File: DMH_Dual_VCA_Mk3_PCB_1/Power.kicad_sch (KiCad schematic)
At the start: 14 parts, among them J0 Conn_01x01, J100 IDC_02x05, U1 TL074, U2 TL074

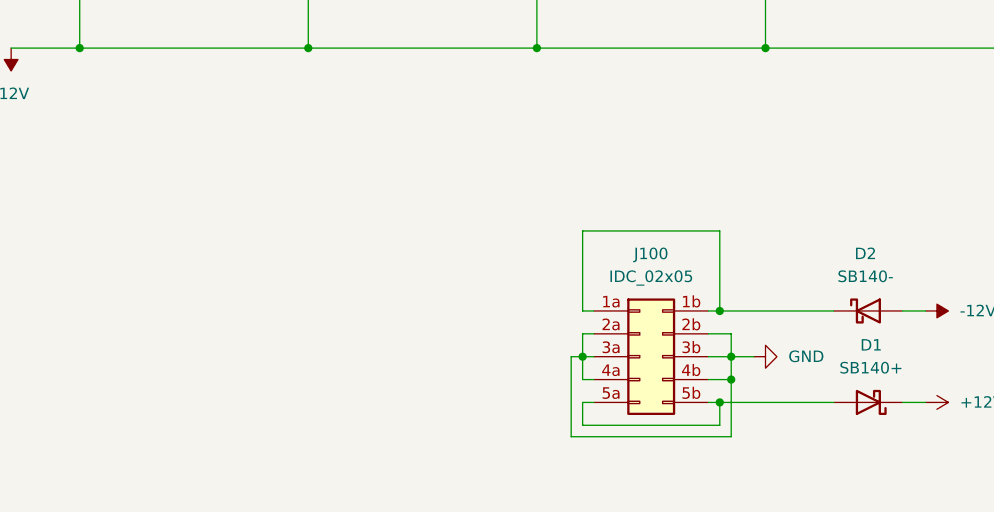
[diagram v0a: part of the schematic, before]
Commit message: Mode switching design in progress
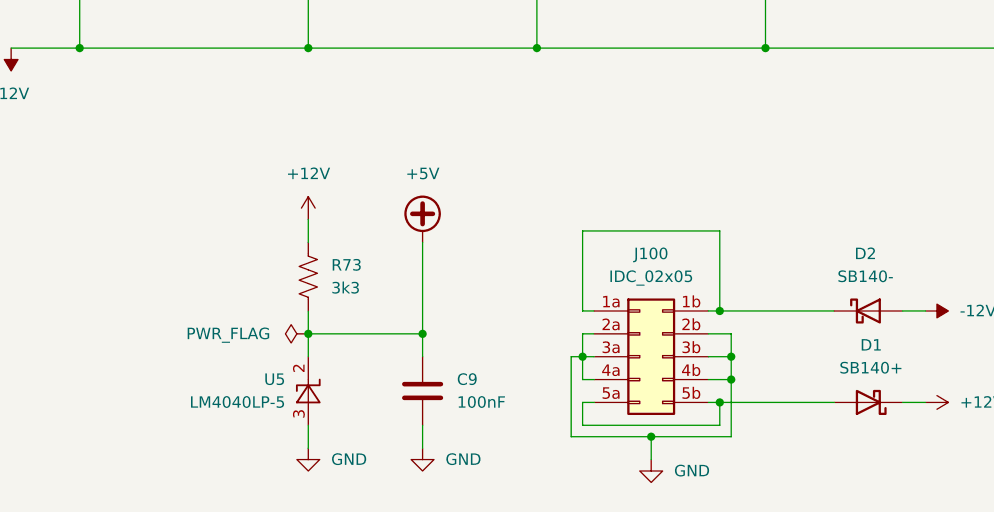
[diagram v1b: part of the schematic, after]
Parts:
- added C9: 100nF, Capacitor_THT:C_Disc_D4.3mm_W1.9mm_P5.00mm, symbol Device:C
- added R73: 3k3, Resistor_THT:R_Axial_DIN0207_L6.3mm_D2.5mm_P7.62mm_Horizontal, symbol Device:R_US
- added U5: LM4040LP-5, Package_TO_SOT_THT:TO-92_Inline, symbol Reference_Voltage:LM4040LP-5
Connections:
- net +12V: now also R73.2
- net GND: now also C9.2, U5.3 (A)
- new net +5V: C9.1, R73.1, U5.2 (K)

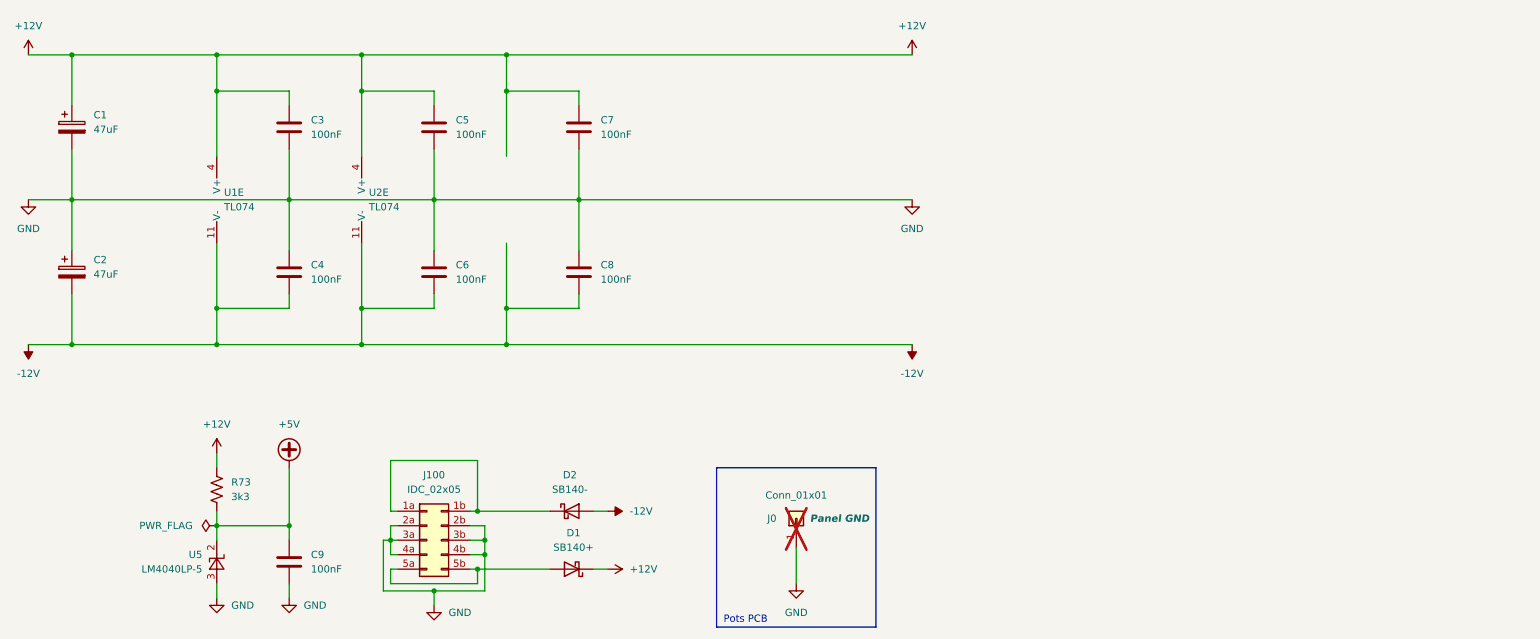
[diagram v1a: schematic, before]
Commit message: 2nd VCA design done
Clipping design in progress
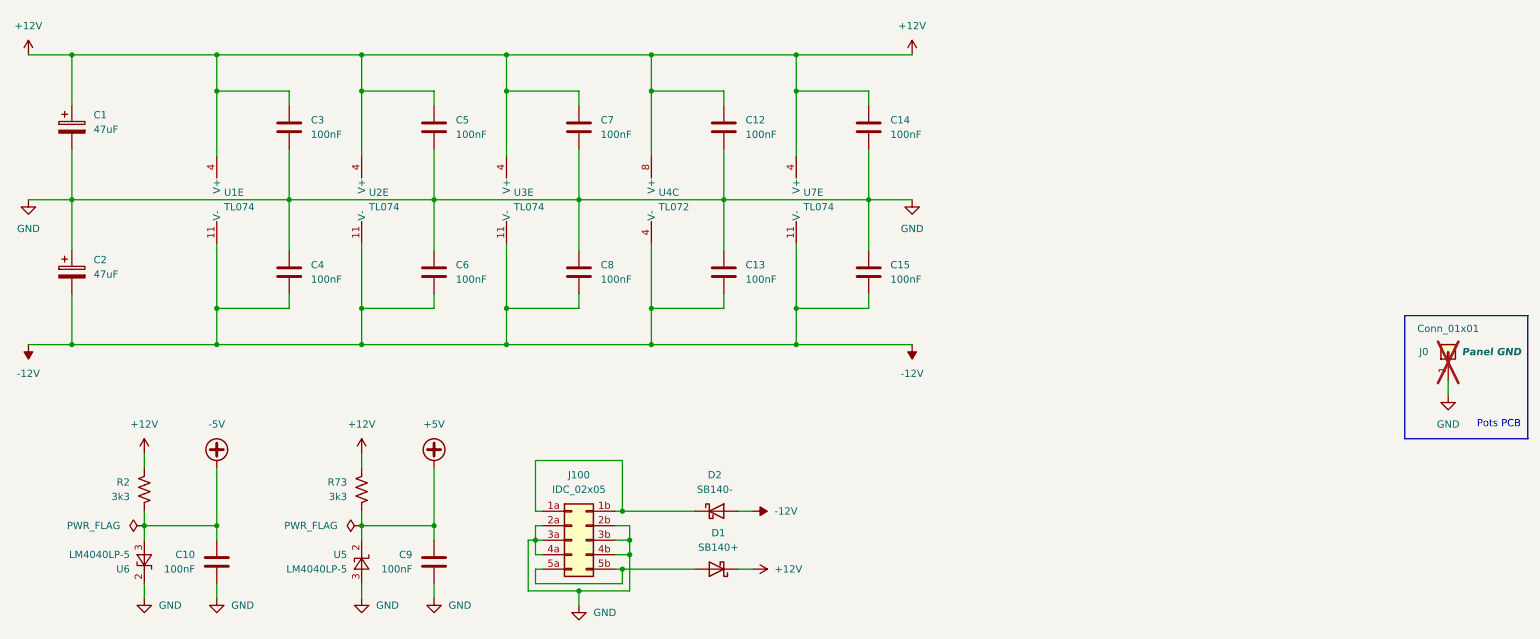
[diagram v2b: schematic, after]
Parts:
- added C10, C12, C13, C14, C15: 100nF, Capacitor_THT:C_Disc_D4.3mm_W1.9mm_P5.00mm, symbol Device:C
- added R2: 3k3, Resistor_THT:R_Axial_DIN0207_L6.3mm_D2.5mm_P7.62mm_Horizontal, symbol Device:R_US
- added U3, U7: TL074, Package_DIP:DIP-14_W7.62mm_Socket, symbol Amplifier_Operational:TL074
- added U4: TL072, Package_DIP:DIP-8_W7.62mm_Socket, symbol Amplifier_Operational:TL072
- added U6: LM4040LP-5, Package_TO_SOT_THT:TO-92_Inline, symbol Reference_Voltage:LM4040LP-5
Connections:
- net +12V: now also C12.1, C14.1, R2.2, U3.4 (V+), U4.8 (V+), U7.4 (V+)
- net -12V: now also C13.2, C15.2, U3.11 (V-), U4.4 (V-), U7.11 (V-)
- net GND: now also C10.2, C12.2, C13.1, C14.2, C15.1, U6.2 (K)
- new net -5V: C10.1, R2.1, U6.3 (A)
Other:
- moved on the sheet: C9, D1, D2, J0, J100, R73, U5

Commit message: Designed clip and dist circuit
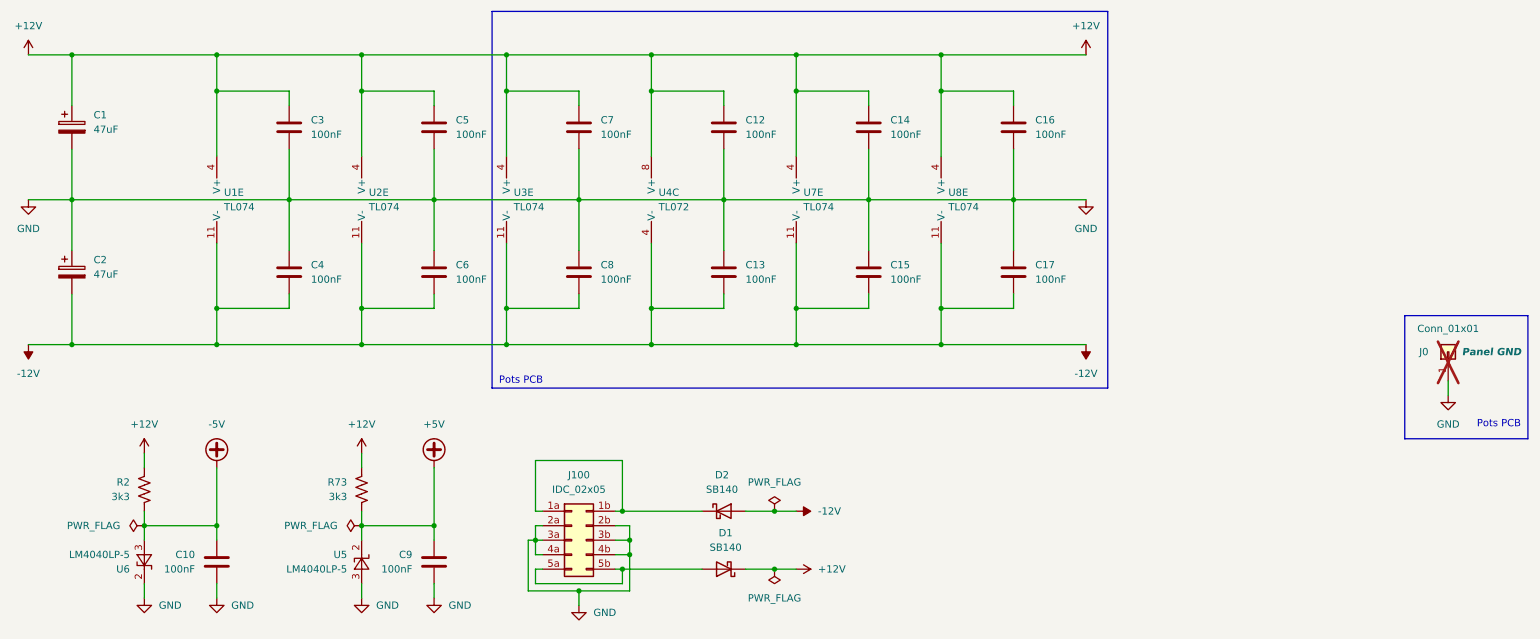
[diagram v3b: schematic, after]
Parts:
- added C16, C17: 100nF, Capacitor_THT:C_Disc_D4.3mm_W1.9mm_P5.00mm, symbol Device:C
- added U8: TL074, Package_DIP:DIP-14_W7.62mm_Socket, symbol Amplifier_Operational:TL074
- D1: value SB140+ -> SB140; symbol SynthStuff:Power_Bus_Schotty_+ -> Diode:SB140
- D2: value SB140- -> SB140; symbol SynthStuff:Power_Bus_Schotty_- -> Diode:SB140
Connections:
- net +12V: now also C16.1, U8.4 (V+)
- net -12V: now also C17.2, U8.11 (V-)
- net GND: now also C16.2, C17.1
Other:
- moved on the sheet: D1, D2

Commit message: Added clipping LED to schematic
Still need to add to Panel
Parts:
- U4: value TL072 -> TL074; footprint Package_DIP:DIP-8_W7.62mm_Socket -> Package_DIP:DIP-14_W7.62mm_Socket; symbol Amplifier_Operational:TL072 -> Amplifier_Operational:TL074
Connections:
- net +12V: now also U4.4 (V+); no longer U4.8 (V+)
- net -12V: now also U4.11 (V-); no longer U4.4 (V-)
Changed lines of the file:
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@@
 	)
 	(symbol
-		(lib_id "Amplifier_Operational:TL072")
+		(lib_id "Amplifier_Operational:TL074")
 		(at 129.54 120.65 0)
-		(unit 3)
-		(exclude_from_sim no)
-		(in_bom yes)
-		(on_board no)
+		(unit 5)
+		(exclude_from_sim no)
+		(in_bom yes)
+		(on_board yes)
 		(dnp no)
 		(fields_autoplaced yes)
 		(property "Reference" "U4"
-			(at 128.27 119.3799 0)
-			(effects
-				(font
-					(size 1.27 1.27)
-				)
-				(justify left)
-			)
-		)
-		(property "Value" "TL072"
-			(at 128.27 121.9199 0)
-			(effects
-				(font
-					(size 1.27 1.27)
-				)
-				(justify left)
-			)
-		)
-		(property "Footprint" "Package_DIP:DIP-8_W7.62mm_Socket"
+			(at 129.54 110.49 0)
+			(effects
+				(font
+					(size 1.27 1.27)
+				)
+			)
+		)
+		(property "Value" "TL074"
+			(at 129.54 113.03 0)
+			(effects
+				(font
+					(size 1.27 1.27)
+				)
+			)
+		)
+		(property "Footprint" "Package_DIP:DIP-14_W7.62mm_Socket"
+			(at 128.27 118.11 0)
+			(effects
+				(font
+					(size 1.27 1.27)
+				)
+				(hide yes)
+			)
+		)
+		(property "Datasheet" "http://www.ti.com/lit/ds/symlink/tl071.pdf"
+			(at 130.81 115.57 0)
+			(effects
+				(font
+					(size 1.27 1.27)
+				)
+				(hide yes)
+			)
+		)
+		(property "Description" "Quad Low-Noise JFET-Input Operational Amplifiers, DIP-14/SOIC-14"
 			(at 129.54 120.65 0)
 			(effects
@@
 			)
 		)
-		(property "Datasheet" "http://www.ti.com/lit/ds/symlink/tl071.pdf"
+		(property "Function" ""
 			(at 129.54 120.65 0)
 			(effects
@@
 					(size 1.27 1.27)
 				)
-				(hide yes)
-			)
-		)
-		(property "Description" "Dual Low-Noise JFET-Input Operational Amplifiers, DIP-8/SOIC-8"
-			(at 129.54 120.65 0)
-			(effects
-				(font
-					(size 1.27 1.27)
-				)
-				(hide yes)
 			)
 		)
@@
 		(pin "4"
 		)
+		(pin "13"
+		)
+		(pin "10"
+		)
+		(pin "9"
+		)
+		(pin "12"
+		)
+		(pin "14"
+		)
+		(pin "11"
+		)
 		(instances
 			(project ""
 				(path "/58f4306d-5387-4983-bb08-41a2313fd315/0cdf34b2-39cd-4d9e-981a-97cd34791509"
 					(reference "U4")
-					(unit 3)
+					(unit 5)
 				)
 			)
@@
 		(exclude_from_sim no)
 		(in_bom yes)
-		(on_board no)
-		(dnp no)
-		(fields_autoplaced yes)
+		(on_board yes)
+		(dnp no)
+		(fields_autoplaced yes)

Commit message: Improved clipping indicator
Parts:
- removed U4: TL074, Package_DIP:DIP-14_W7.62mm_Socket, symbol Amplifier_Operational:TL074
- added U4: TL072, Package_DIP:DIP-8_W7.62mm_Socket, symbol Amplifier_Operational:TL072
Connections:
- net +12V: now also U4.8 (V+)
- net -12V: now also U4.4 (V-)
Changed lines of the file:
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@@
+	)
+	(symbol
+		(lib_id "Amplifier_Operational:TL072")
+		(at 129.54 120.65 0)
+		(unit 3)
+		(exclude_from_sim no)
+		(in_bom yes)
+		(on_board no)
+		(dnp no)
+		(fields_autoplaced yes)
+		(property "Reference" "U4"
+			(at 128.27 119.3799 0)
+			(effects
+				(font
+					(size 1.27 1.27)
+				)
+				(justify left)
+			)
+		)
+		(property "Value" "TL072"
+			(at 128.27 121.9199 0)
+			(effects
+				(font
+					(size 1.27 1.27)
+				)
+				(justify left)
+			)
+		)
+		(property "Footprint" "Package_DIP:DIP-8_W7.62mm_Socket"
+			(at 129.54 120.65 0)
+			(effects
+				(font
+					(size 1.27 1.27)
+				)
+				(hide yes)
+			)
+		)
+		(property "Datasheet" "http://www.ti.com/lit/ds/symlink/tl071.pdf"
+			(at 129.54 120.65 0)
+			(effects
+				(font
+					(size 1.27 1.27)
+				)
+				(hide yes)
+			)
+		)
+		(property "Description" "Dual Low-Noise JFET-Input Operational Amplifiers, DIP-8/SOIC-8"
+			(at 129.54 120.65 0)
+			(effects
+				(font
+					(size 1.27 1.27)
+				)
+				(hide yes)
+			)
+		)
+		(pin "2"
+		)
+		(pin "8"
+		)
+		(pin "3"
+		)
+		(pin "1"
+		)
+		(pin "5"
+		)
+		(pin "6"
+		)
+		(pin "7"
+		)
+		(pin "4"
+		)
+		(instances
+			(project ""
+				(path "/58f4306d-5387-4983-bb08-41a2313fd315/0cdf34b2-39cd-4d9e-981a-97cd34791509"
+					(reference "U4")
+					(unit 3)
+				)
+			)
+		)
 	)
 	(symbol
@@
 				)
 			)
-		)
-	)
-	(symbol
-		(lib_id "Amplifier_Operational:TL074")
-		(at 129.54 120.65 0)
-		(unit 5)
-		(exclude_from_sim no)
-		(in_bom yes)
-		(on_board no)
-		(dnp no)
-		(fields_autoplaced yes)
-		(property "Reference" "U4"
-			(at 129.54 110.49 0)
-			(effects
-				(font
-					(size 1.27 1.27)
-				)
-			)
-		)
-		(property "Value" "TL074"
-			(at 129.54 113.03 0)
-			(effects
-				(font
-					(size 1.27 1.27)
-				)
-			)
-		)
-		(property "Footprint" "Package_DIP:DIP-14_W7.62mm_Socket"
-			(at 128.27 118.11 0)
-			(effects
-				(font
-					(size 1.27 1.27)
-				)
-				(hide yes)
-			)
-		)
-		(property "Datasheet" "http://www.ti.com/lit/ds/symlink/tl071.pdf"
-			(at 130.81 115.57 0)
-			(effects
-				(font
-					(size 1.27 1.27)
-				)
-				(hide yes)
-			)
-		)
-		(property "Description" "Quad Low-Noise JFET-Input Operational Amplifiers, DIP-14/SOIC-14"
-			(at 129.54 120.65 0)
-			(effects
-				(font
-					(size 1.27 1.27)
-				)
-				(hide yes)
-			)
-		)
-		(property "Function" ""
-			(at 129.54 120.65 0)
-			(effects
-				(font
-					(size 1.27 1.27)
-				)
-			)
-		)
-		(pin "1"
-		)
-		(pin "7"
-		)
-		(pin "2"
-		)
-		(pin "3"
-		)
-		(pin "5"
-		)
-		(pin "6"
-		)
-		(pin "8"
-		)
-		(pin "4"
-		)
-		(pin "13"
-		)
-		(pin "10"
-		)
-		(pin "9"
-		)
-		(pin "12"
-		)
-		(pin "14"
-		)
-		(pin "11"
-		)
-		(instances
-			(project ""
-				(path "/58f4306d-5387-4983-bb08-41a2313fd315/0cdf34b2-39cd-4d9e-981a-97cd34791509"
-					(reference "U4")
-					(unit 5)
-				)
-			)
